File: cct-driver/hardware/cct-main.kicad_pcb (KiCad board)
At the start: 2 copper layers, 130 x 164 mm, 217 parts, among them J1 C707824, J10 C37815, J11 C474923, J2 C165948, J3 C441333, J4 C441333, J5 C441333, J6 C441333, J7 C441333, J8 C441333, J9 C2906270, Q1 C3281500, Q10 C2890395, Q11 C2890395, Q12 C2890395, Q13 C2890395, Q14 C2890395, Q15 C2890395, Q16 C2890395, Q17 C2890395, Q18 C2890395, Q2 C3281500, Q3 C20526, Q4 C2146, Q5 C2146, Q6 C20526, Q7 C2890395, Q8 C2890395, Q9 C2890395, SW1 C318884, SW2 C318884, U1 C2864837, U2 C524806, U3 C6186, U4 C701341, U5 C84681, U6 C52140501, U7 C52140501

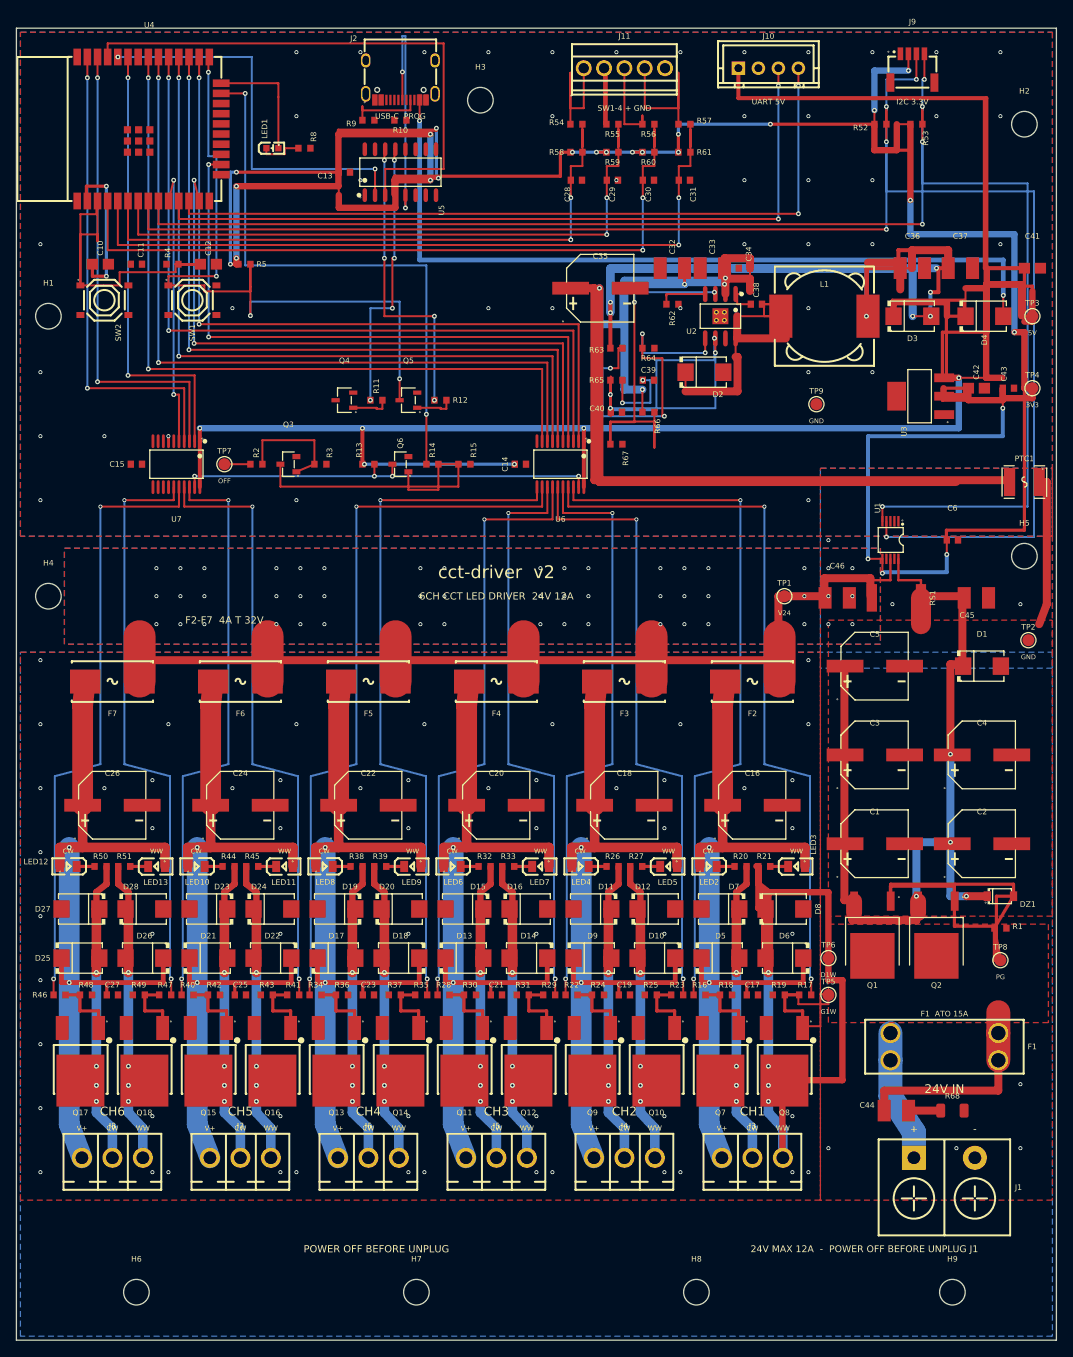
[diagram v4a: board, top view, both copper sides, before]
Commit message: v2 布线:栅格化改成按真实距离判,间距违规 13 → 5;地覆铜改成每层一整块
**栅格化原来是拿包围盒粗暴地涂**,一涂就多堵掉最多两格(0.5mm)。
而 Type-C 那排脚的缝隙本来就只有 0.35mm —— 多堵一点就再也搜不出路来。
改成逐格按「格点到障碍矩形的真实距离」判之后,USB 那几条才钻得进连接器身子底下
(v1 也是这么走的:0.20mm 细线从 y≈4 那一层钻上去)。

**地覆铜从五块互相重叠改成每层一整块,形状里刻意留一道口子:**

    ┌──────────────────┐
    │     逻辑地        │
    ├────────────┬─────┤  y63.5
    │ 脊椎带,无地│ D0  │  ← 唯一通路在 x>100.5(RS1 那一侧)
    ├────────────┤     │  y78
    │     功率地        │
    └────────────┴─────┘

早先拆成五块,KiCad 认为优先级不同的同网覆铜只是「贴着」不是「连着」,
DRC 一直报十几条「覆铜与覆铜未连接」。一整块 + 一道口子,单点接地保住了,
连通性判定也不再误报。另外打开了覆铜的**孤岛清除**:走线把大铜面切碎后
难免留下没连上的小铜片,留着既是天线又会被逐块报未连接。

顺带按板规校准了布线间距:粗线走 PWR* 类要 0.25、细线按 Default 的 0.2
(早先图省事用了 0.18,那是真的违规);迷宫布线两端补到焊盘的那两小截也纳入检查。

    走线 1149 段 · 过孔 514 颗 · 覆铜 14 块
    未连接 29 · 间距 5 · **短路 1**(V3P3 与 DTR 在 U5 脚边,还没查清,如实记着)
    网表与原理图 525 条零差异

Co-Authored-By: Claude <noreply@anthropic.com>
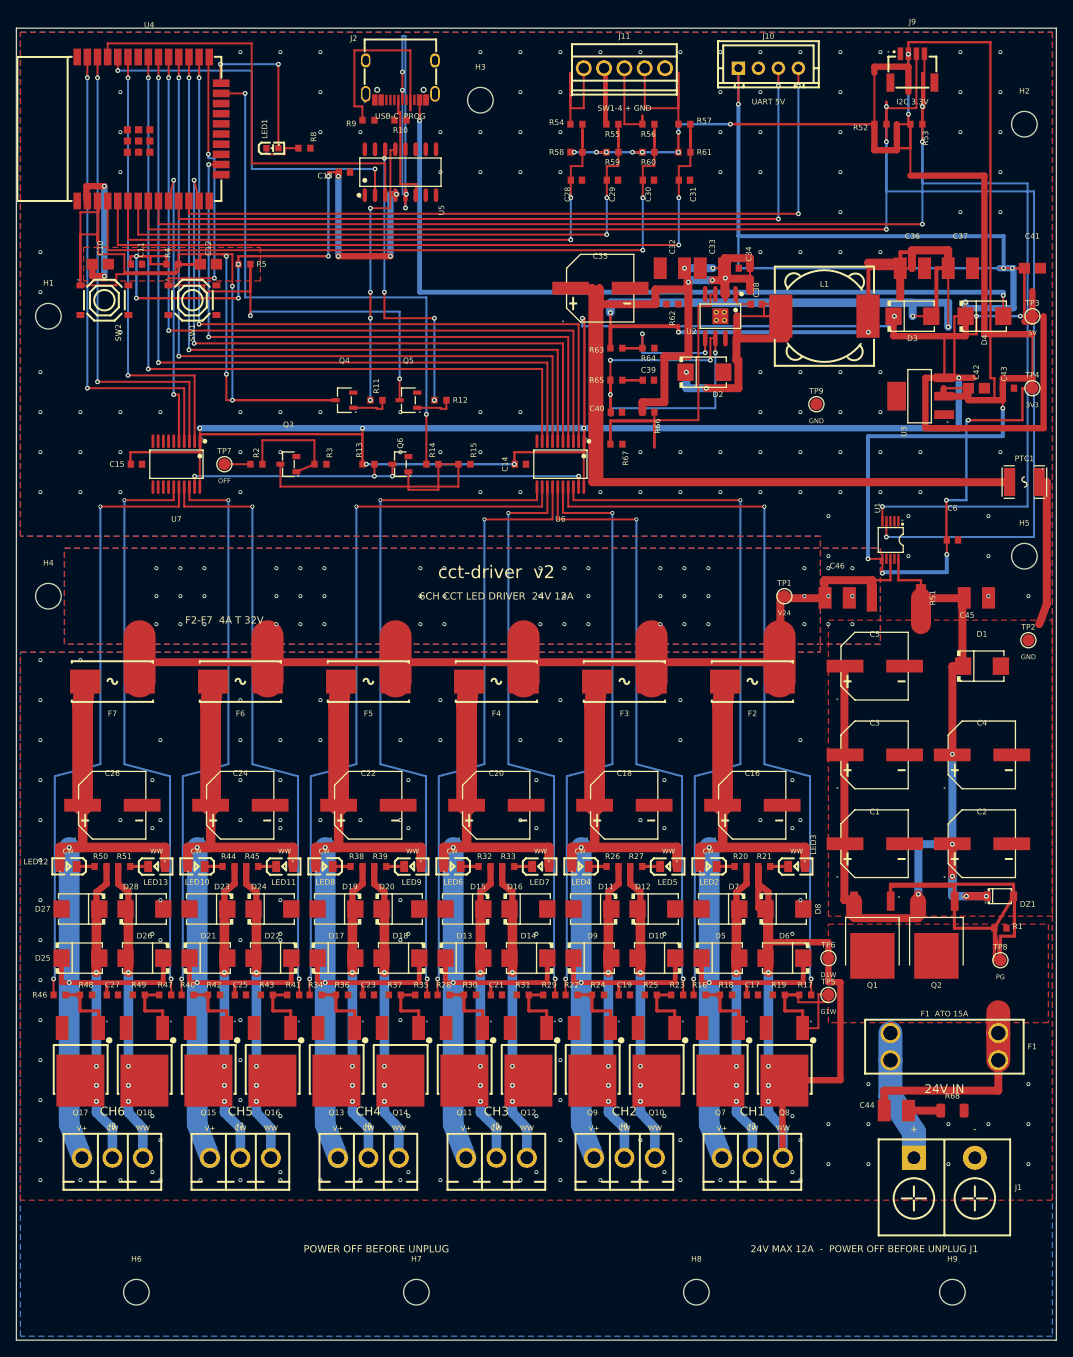
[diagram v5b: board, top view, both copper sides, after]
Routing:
- net V5_SYS: track 391.5 -> 511.9 mm, vias 6 -> 14
- net EN: track 56.7 -> 153.3 mm, vias 0 -> 4
- net USB_DM: track 0.00 -> 28.4 mm
- net FB_5V: track 43.9 -> 22.6 mm, vias 4 -> 2
- net CC1: track 9.53 -> 25.5 mm
- net USB_DP: track 31.5 -> 46.4 mm, vias 2 -> 4
- net U0TXD: track 70.0 -> 55.4 mm
- net CH1_WW_D: track 111.2 -> 97.6 mm
- net V24_LOGIC: track 246.4 -> 233.2 mm
- net V5_BUCK: track 213.4 -> 201.5 mm, vias 7 -> 5
- net I2C_SCL: track 205.3 -> 214.1 mm, vias 5 -> 4
- net V24_PROT: track 140.7 -> 148.3 mm, vias 4 -> 6
- net RT_CLK: track 6.12 -> 0.00 mm
- net LED_STATUS: track 15.3 -> 20.4 mm, vias 0 -> 2
- net IO0: track 89.3 -> 86.5 mm
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- added copper zone on F.Cu, net V3P3

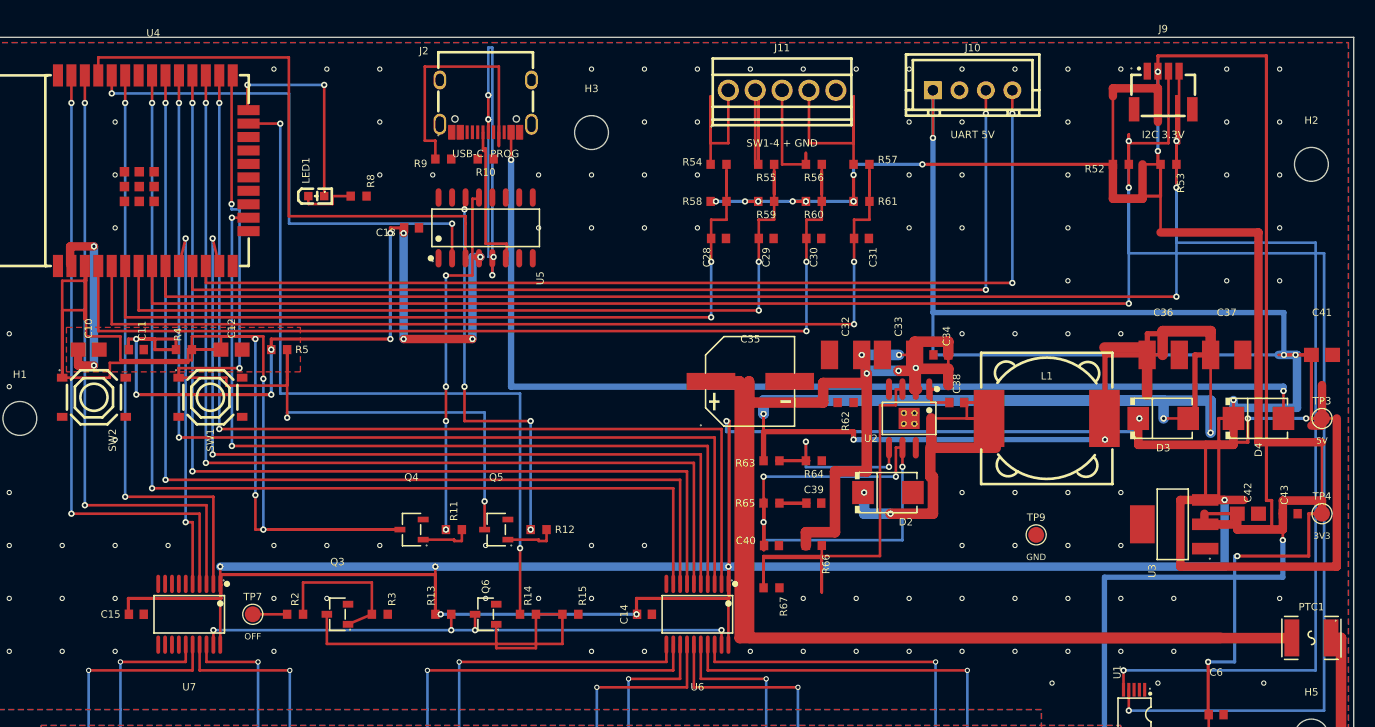
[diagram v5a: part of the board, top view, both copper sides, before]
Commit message: v2 布线:最后一处短路查清并改掉 —— 3V3 干线在 U5 脚边不能用 0.8mm
查法是把那两条线从板文件里逐条打出来看:V3P3 那一段**宽 0.8mm**,
两端圆头一伸就盖到 46.85,而 DTR 的竖线右边缘在 46.875 —— 差 0.025mm,实打实压上。
把 3V3 / 5V 干线的宽度从 0.8 收到 0.4:U5 那排脚只隔 0.5mm,0.8mm 的线**根本塞不进去**,
而这两条只走几百毫安,0.4mm 绰绰有余。

    走线 1169 段 · 过孔 522 颗 · 覆铜 14 块
    **短路 0 · 走线交叉 1 · 间距 6**(其中 4 条是 J2/U2 封装自带的)
    未连接 28 条(今天开工时 133)
    网表与原理图 525 条零差异

Co-Authored-By: Claude <noreply@anthropic.com>
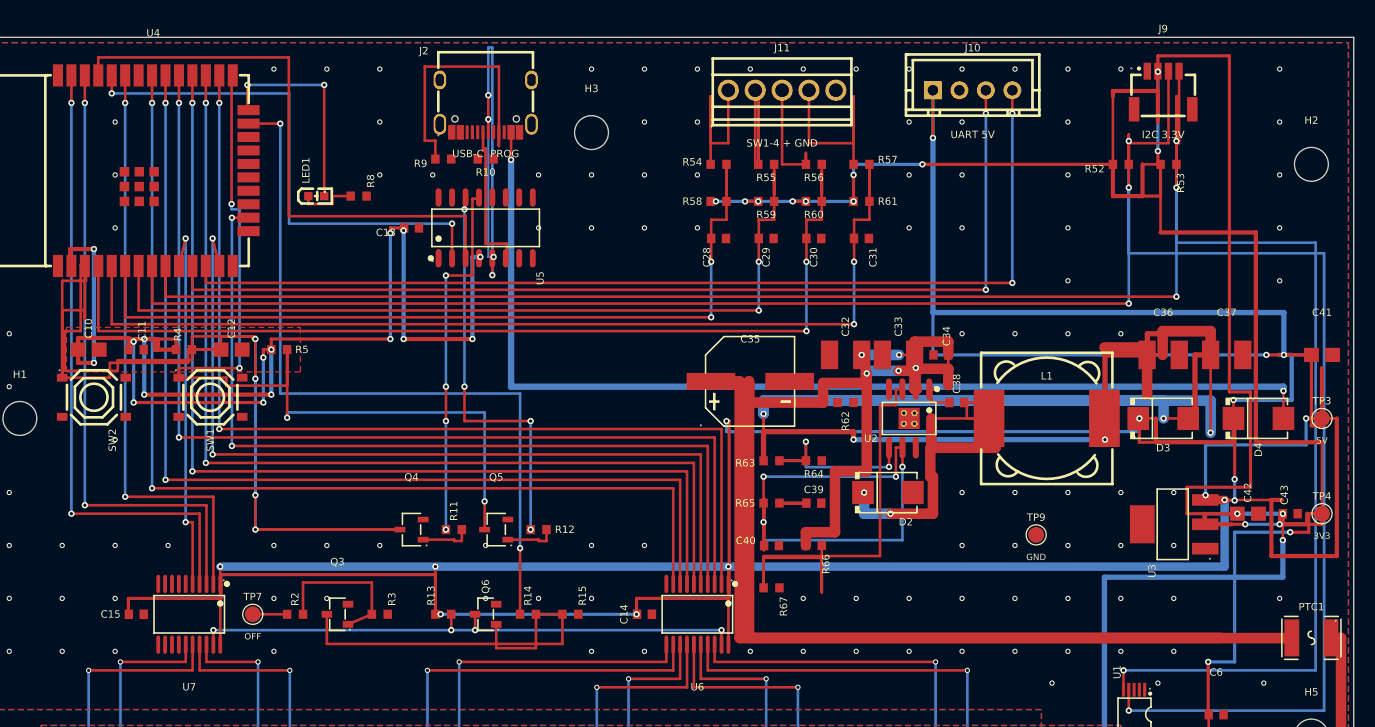
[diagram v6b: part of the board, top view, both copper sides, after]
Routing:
- net V3P3: track 433.2 -> 471.2 mm, vias 28 -> 36
- net V5_SYS: track 511.9 -> 500.1 mm, vias 14 -> 16
- net EN: track 153.3 -> 159.3 mm
- net GND: vias 238 -> 236
